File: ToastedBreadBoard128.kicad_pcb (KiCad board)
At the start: 2 copper layers, 53.3 x 176.5 mm, 11 parts, among them J1 Conn_02x20_Odd_Even, J2 Conn_02x20_Odd_Even, J3 Conn_02x20_Odd_Even, J4 Conn_02x20_Odd_Even, J5 Conn_02x20_Odd_Even, J6 Conn_02x20_Odd_Even, U1 DIL126

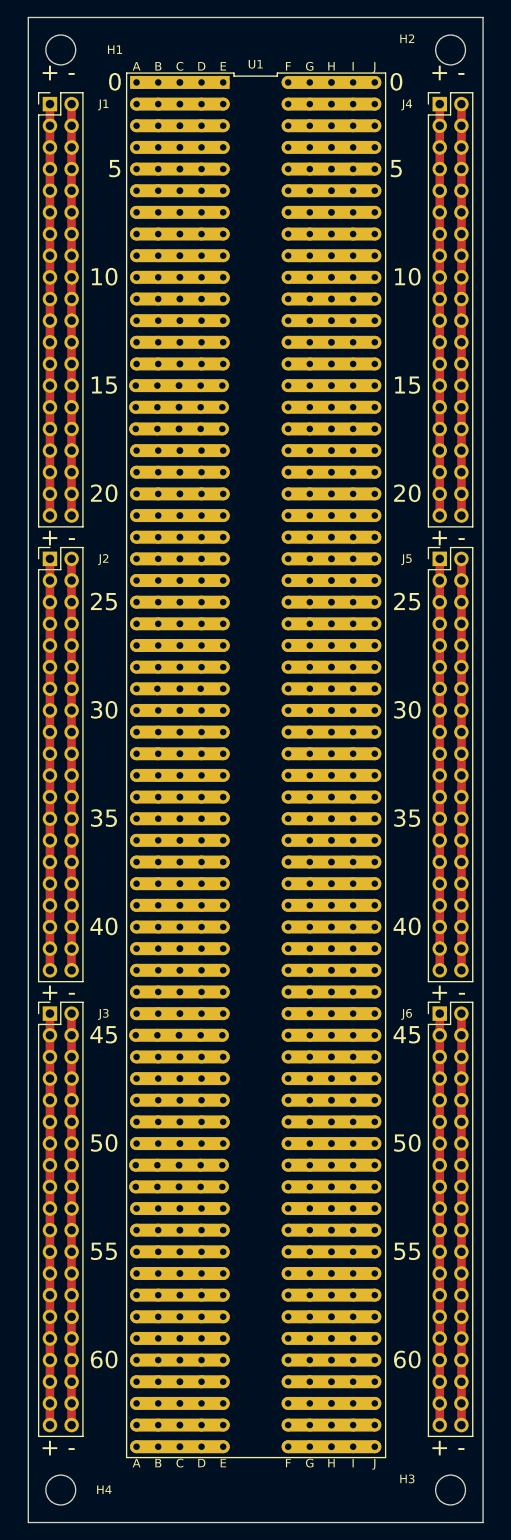
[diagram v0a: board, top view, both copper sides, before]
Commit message: Make all holes the same size.
Signed-off-by: John Bradley <flypie@rocketmail.com>
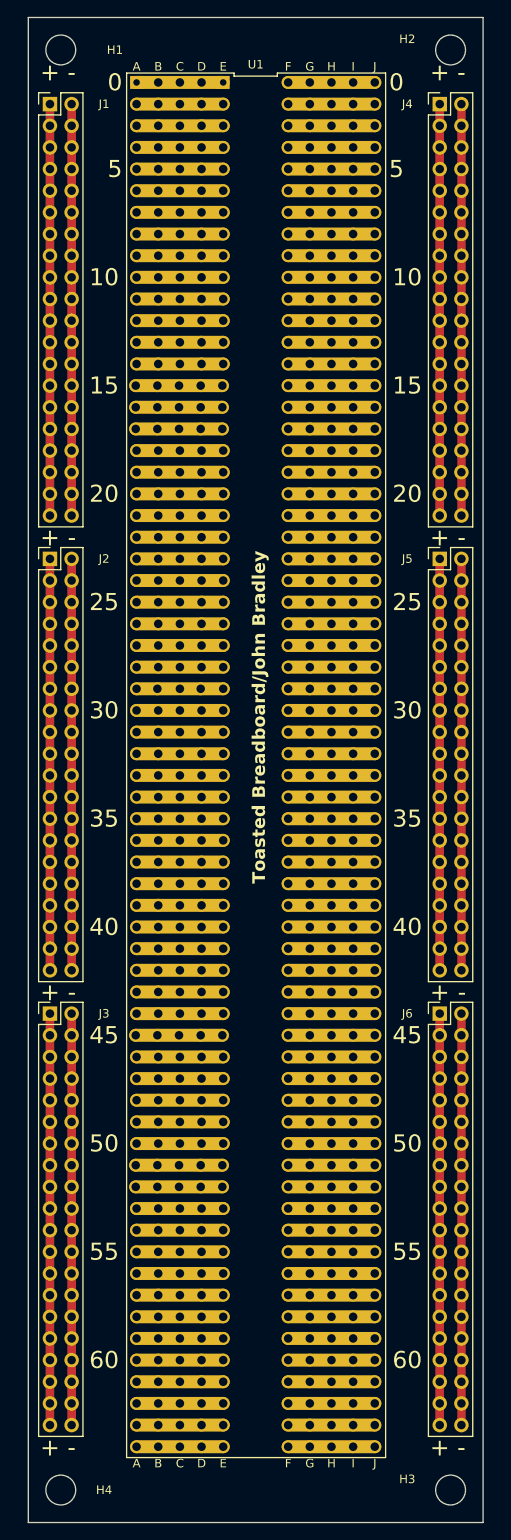
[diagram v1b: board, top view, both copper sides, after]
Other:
- board text added: "Toasted Breadboard/John Bradley"

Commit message: Correct Width.
Signed-off-by: John Bradley <flypie@rocketmail.com>
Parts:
- moved H2 1.27 mm to (152.4, 25.4)
- moved H3 1.27 mm to (152.4, 194.3)
- moved H1 1.27 mm to (104.1, 25.4)
- moved H4 1.27 mm to (104.1, 194.3)
- moved J1 1.27 mm to (102.9, 31.8)
- moved J2 1.27 mm to (102.9, 85.1)
- moved J3 1.27 mm to (102.9, 138.4)
- moved J4 1.27 mm to (151.1, 31.8)
- moved J5 1.27 mm to (151.1, 85.1)
- moved J6 1.27 mm to (151.1, 138.4)
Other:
- board size 53.3 x 176.5 mm -> 55.9 x 176.5 mm
